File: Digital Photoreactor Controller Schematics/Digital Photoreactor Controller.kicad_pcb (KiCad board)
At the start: 2 copper layers, 82.3 x 30.5 mm, 16 parts, among them J1 LDD-1500L, J2 Conn_01x02, J3 Barrel_Jack, J4 Conn_01x04, J5 Conn_01x04, J6 Barrel_Jack, J7 Conn_01x04, U1 ATtiny85-20PU

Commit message: Updated PCB routing
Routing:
- net PWM_LED: track 39.2 -> 41.4 mm

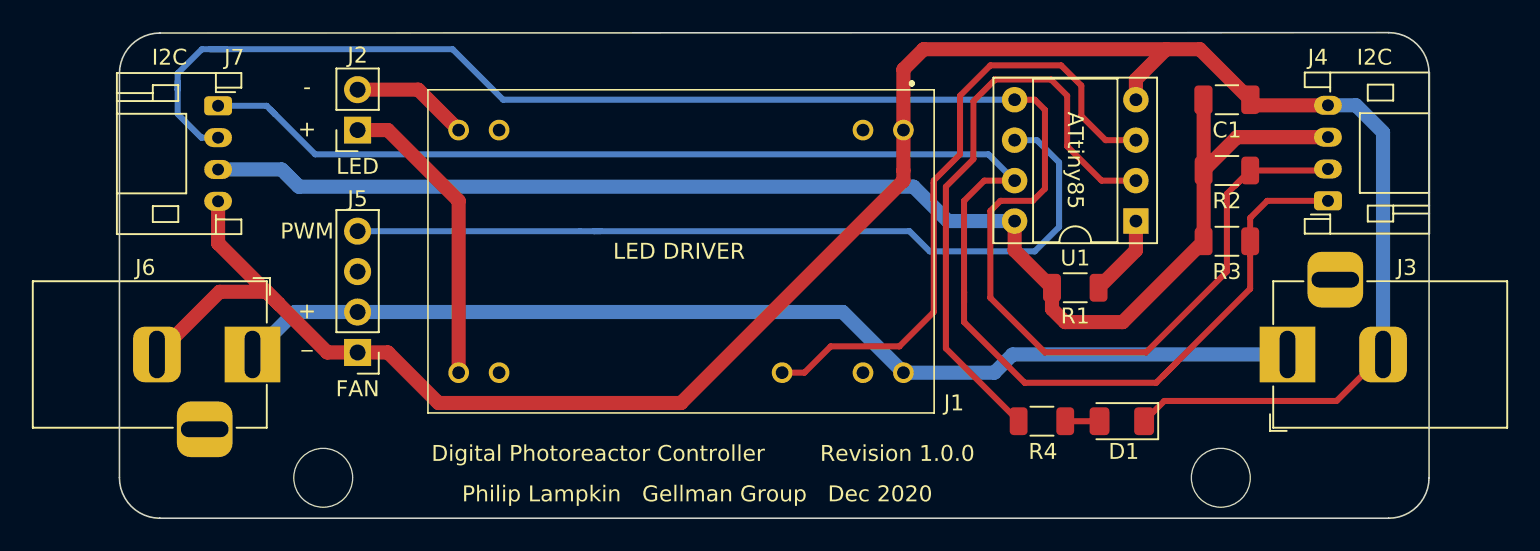
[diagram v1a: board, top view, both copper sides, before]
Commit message: Updated drill marks and edgecuts to be more uniform
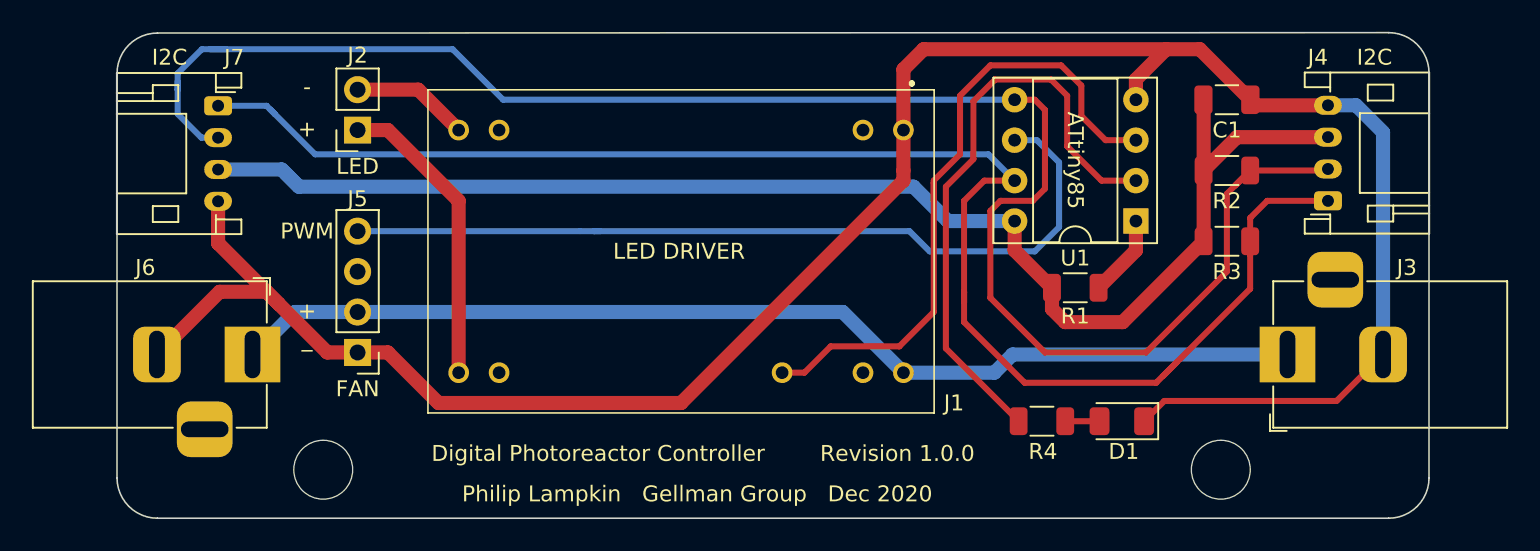
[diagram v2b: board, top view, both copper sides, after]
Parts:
- moved REF** 0.51 mm to (150.4, 116.8)
- moved REF** 0.51 mm to (94.0, 116.8)
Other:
- board size 82.3 x 30.5 mm -> 82.4 x 30.5 mm
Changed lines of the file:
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@@
   )
   (setup
-    (last_trace_width 0.381)
+    (last_trace_width 0.25)
     (user_trace_width 0.381)
     (user_trace_width 0.889)
@@
       (outputformat 1)
       (mirror false)
-      (drillshape 1)
+      (drillshape 0)
       (scaleselection 1)
       (outputdirectory ""))
@@
       (effects (font (size 0.8 0.8) (thickness 0.12)))
     )
-    (pad 2 smd roundrect (at 1.4625 0 180) (size 1.125 1.75) (layers F.Cu F.Paste F.Mask) (roundrect_rratio 0.222222)
+    (pad 2 smd roundrect (at 1.4625 0 180) (size 1.125 1.75) (layers F.Cu F.Paste F.Mask) (roundrect_rratio 0.2222213333333333)
       (net 16 INDICATOR))
-    (pad 1 smd roundrect (at -1.4625 0 180) (size 1.125 1.75) (layers F.Cu F.Paste F.Mask) (roundrect_rratio 0.222222)
+    (pad 1 smd roundrect (at -1.4625 0 180) (size 1.125 1.75) (layers F.Cu F.Paste F.Mask) (roundrect_rratio 0.2222213333333333)
       (net 17 "Net-(D1-Pad2)"))
     (model ${KISYS3DMOD}/Resistor_SMD.3dshapes/R_1206_3216Metric.wrl
@@
     (pad 2 thru_hole oval (at 2 0 270) (size 1.2 1.75) (drill 0.75) (layers *.Cu *.Mask)
       (net 4 SDA))
-    (pad 1 thru_hole roundrect (at 0 0 270) (size 1.2 1.75) (drill 0.75) (layers *.Cu *.Mask) (roundrect_rratio 0.208333)
+    (pad 1 thru_hole roundrect (at 0 0 270) (size 1.2 1.75) (drill 0.75) (layers *.Cu *.Mask) (roundrect_rratio 0.2083325)
       (net 5 SCL))
     (model ${KISYS3DMOD}/Connector_JST.3dshapes/JST_PH_S4B-PH-K_1x04_P2.00mm_Horizontal.wrl
@@
   )
   (module MountingHole:MountingHole_3.7mm (layer F.Cu)
-    (at 150.368 117.348 180)
+    (at 150.368 116.84 180)
     (descr "Mounting Hole 3.7mm, no annular")
     (tags "mounting hole 3.7mm no annular")
@@
   )
   (module MountingHole:MountingHole_3.7mm (layer F.Cu)
-    (at 93.98 117.348 180)
+    (at 93.98 116.84 180)
     (descr "Mounting Hole 3.7mm, no annular")
     (tags "mounting hole 3.7mm no annular")
@@
       (effects (font (size 0.8 0.8) (thickness 0.12)))
     )
-    (pad 2 smd roundrect (at 1.4625 0) (size 1.125 1.75) (layers F.Cu F.Paste F.Mask) (roundrect_rratio 0.222222)
+    (pad 2 smd roundrect (at 1.4625 0) (size 1.125 1.75) (layers F.Cu F.Paste F.Mask) (roundrect_rratio 0.2222213333333333)
       (net 5 SCL))
-    (pad 1 smd roundrect (at -1.4625 0) (size 1.125 1.75) (layers F.Cu F.Paste F.Mask) (roundrect_rratio 0.222222)
+    (pad 1 smd roundrect (at -1.4625 0) (size 1.125 1.75) (layers F.Cu F.Paste F.Mask) (roundrect_rratio 0.2222213333333333)
       (net 3 +5V))
     (model ${KISYS3DMOD}/Resistor_SMD.3dshapes/R_1206_3216Metric.wrl
@@
       (effects (font (size 0.8 0.8) (thickness 0.12)))
     )
-    (pad 2 smd roundrect (at 1.4625 0) (size 1.125 1.75) (layers F.Cu F.Paste F.Mask) (roundrect_rratio 0.222222)
+    (pad 2 smd roundrect (at 1.4625 0) (size 1.125 1.75) (layers F.Cu F.Paste F.Mask) (roundrect_rratio 0.2222213333333333)
       (net 4 SDA))
-    (pad 1 smd roundrect (at -1.4625 0) (size 1.125 1.75) (layers F.Cu F.Paste F.Mask) (roundrect_rratio 0.222222)
+    (pad 1 smd roundrect (at -1.4625 0) (size 1.125 1.75) (layers F.Cu F.Paste F.Mask) (roundrect_rratio 0.2222213333333333)
       (net 3 +5V))
     (model ${KISYS3DMOD}/Resistor_SMD.3dshapes/R_1206_3216Metric.wrl
@@
       (effects (font (size 0.8 0.8) (thickness 0.12)))
     )
-    (pad 2 smd roundrect (at 1.4625 0) (size 1.125 1.75) (layers F.Cu F.Paste F.Mask) (roundrect_rratio 0.222222)
+    (pad 2 smd roundrect (at 1.4625 0) (size 1.125 1.75) (layers F.Cu F.Paste F.Mask) (roundrect_rratio 0.2222213333333333)
       (net 10 "Net-(R1-Pad2)"))
-    (pad 1 smd roundrect (at -1.4625 0) (size 1.125 1.75) (layers F.Cu F.Paste F.Mask) (roundrect_rratio 0.222222)
+    (pad 1 smd roundrect (at -1.4625 0) (size 1.125 1.75) (layers F.Cu F.Paste F.Mask) (roundrect_rratio 0.2222213333333333)
       (net 3 +5V))
     (model ${KISYS3DMOD}/Resistor_SMD.3dshapes/R_1206_3216Metric.wrl
@@
     (pad 2 thru_hole oval (at 2 0 90) (size 1.2 1.75) (drill 0.75) (layers *.Cu *.Mask)
       (net 4 SDA))
-    (pad 1 thru_hole roundrect (at 0 0 90) (size 1.2 1.75) (drill 0.75) (layers *.Cu *.Mask) (roundrect_rratio 0.208333)
+    (pad 1 thru_hole roundrect (at 0 0 90) (size 1.2 1.75) (drill 0.75) (layers *.Cu *.Mask) (roundrect_rratio 0.2083325)
       (net 5 SCL))
     (model ${KISYS3DMOD}/Connector_JST.3dshapes/JST_PH_S4B-PH-K_1x04_P2.00mm_Horizontal.wrl
@@
       (effects (font (size 0.8 0.8) (thickness 0.12)))
     )
-    (pad 2 smd roundrect (at 1.475 0) (size 1.15 1.8) (layers F.Cu F.Paste F.Mask) (roundrect_rratio 0.217391)
-      (net 1 GND))
-    (pad 1 smd roundrect (at -1.475 0) (size 1.15 1.8) (layers F.Cu F.Paste F.Mask) (roundrect_rratio 0.217391)
+    (pad 2 smd roundrect (at 1.475 0) (size 1.15 1.8) (layers F.Cu F.Paste F.Mask) (roundrect_rratio 0.2173904347826087)
+      (net 1 GND))
+    (pad 1 smd roundrect (at -1.475 0) (size 1.15 1.8) (layers F.Cu F.Paste F.Mask) (roundrect_rratio 0.2173904347826087)
       (net 3 +5V))
     (model ${KISYS3DMOD}/Capacitor_SMD.3dshapes/C_1206_3216Metric.wrl
@@
   (gr_arc (start 160.909 117.348) (end 160.909 119.888) (angle -90) (layer Edge.Cuts) (width 0.1))
   (gr_arc (start 160.909 91.9226) (end 163.449 91.9226) (angle -90) (layer Edge.Cuts) (width 0.1))
-  (gr_arc (start 83.7184 91.948) (end 83.7184 89.408) (angle -90) (layer Edge.Cuts) (width 0.1))
-  (gr_line (start 81.1784 117.348) (end 81.1784 91.948) (layer Edge.Cuts) (width 0.1))
-  (gr_arc (start 83.7184 117.348) (end 81.1784 117.348) (angle -90) (layer Edge.Cuts) (width 0.1))
-  (gr_line (start 160.909 119.888) (end 83.7184 119.888) (layer Edge.Cuts) (width 0.1))
+  (gr_arc (start 83.566 91.948) (end 83.566 89.408) (angle -90) (layer Edge.Cuts) (width 0.1))
+  (gr_line (start 81.026 117.348) (end 81.026 91.948) (layer Edge.Cuts) (width 0.1))
+  (gr_arc (start 83.566 117.348) (end 81.026 117.348) (angle -90) (layer Edge.Cuts) (width 0.1))
+  (gr_line (start 160.909 119.888) (end 83.566 119.888) (layer Edge.Cuts) (width 0.1))
   (gr_line (start 163.449 91.9226) (end 163.449 117.348) (layer Edge.Cuts) (width 0.1))
-  (gr_line (start 83.7184 89.408) (end 160.909 89.3826) (layer Edge.Cuts) (width 0.1))
+  (gr_line (start 83.566 89.408) (end 160.909 89.3826) (layer Edge.Cuts) (width 0.1))
   (gr_text _ (at 92.964 110.109 180) (layer F.SilkS)
     (effects (font (size 1 1) (thickness 0.25)))
